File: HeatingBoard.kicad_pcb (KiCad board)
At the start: 2 copper layers, 80 x 60 mm, 107 parts, among them J1 Conn_01x02, J2 Conn_01x06, J3 Conn_01x03, J4 Conn_01x03, J5 Conn_01x05, Q1 T2N7002AK,LM, Q2 DMP3099L, Q3 T2N7002AK,LM, Q4 DMP3099L, Q5 T2N7002AK,LM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

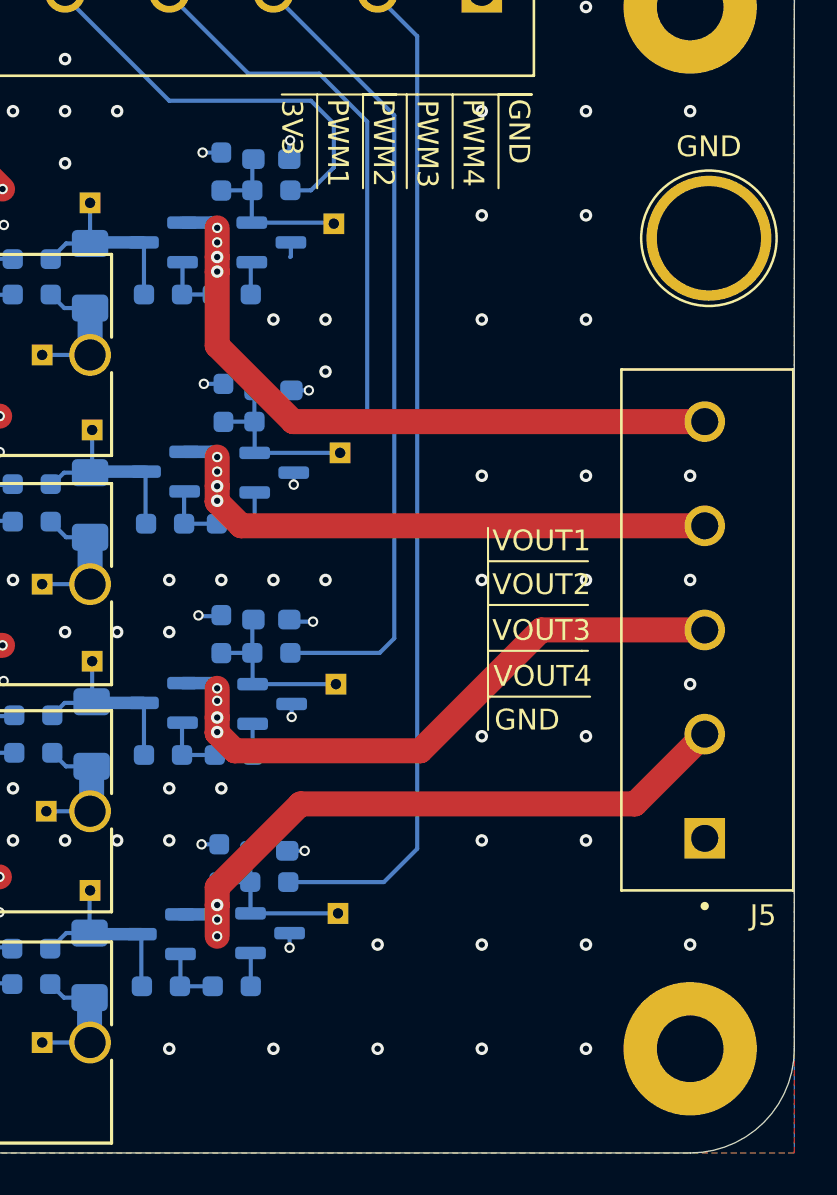
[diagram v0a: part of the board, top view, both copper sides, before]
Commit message: Added QR code and images
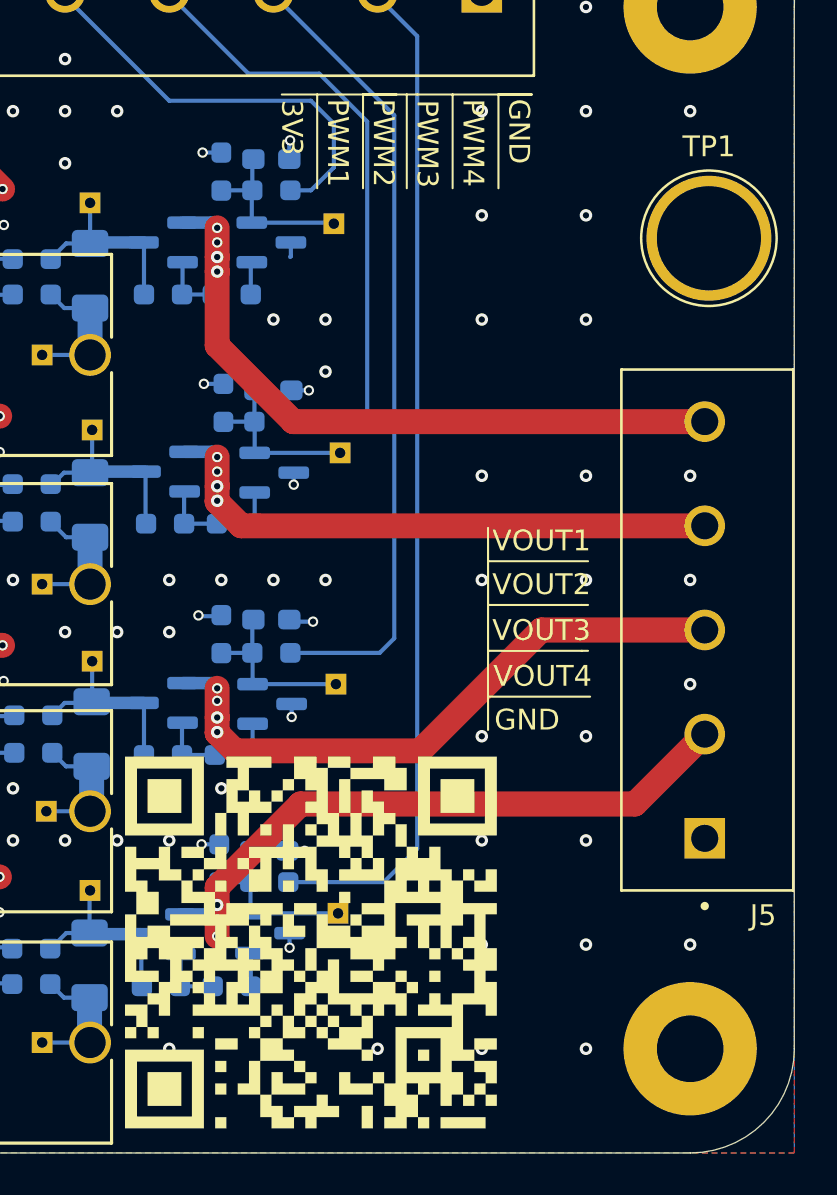
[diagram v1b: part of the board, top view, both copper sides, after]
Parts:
- added H5: QR code, HeatingBoard:QRcode, F.Cu at (166.8, 119.9)
- renumbered GND to TP1
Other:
- board text added: "EE MOD11 - Group B"
- board text added: "Heating Control Board"
